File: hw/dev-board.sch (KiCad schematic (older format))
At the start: 66 parts

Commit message: Removed opamp and tied 3.3v LDO switch to sense pin on DC connector.
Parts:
- removed R? (x2): 10K, symbol R
- removed U?: LM358, symbol LM358
- removed X?: RESONATOR, symbol RESONATOR
- added R?: 10K, symbol R
- added X1: CRYSTAL, Spenduino_CustomFootprints:SMD_Crystal_ABM8G, symbol CRYSTAL
- C1, C2, C3, C4, C5, C6, C7, C8, C9: renamed from C?; footprint (none) -> Capacitors_SMD:C_0603
- C10: renamed from 100n; value C -> 100n; footprint (none) -> Capacitors_SMD:C_0603
- D2, D3, D4: renamed from D?; footprint (none) -> LEDs:LED_0603
- F1: renamed from F?; footprint (none) -> Resistors_SMD:R_1812
- IC2, IC6: renamed from IC?; footprint SO8-200 -> (none)
- IC4, IC7: renamed from IC?; footprint WQFN20 -> (none)
- IC5: renamed from IC?; footprint MLF/QFN32 -> (none)
- L1: renamed from L?; footprint (none) -> Resistors_SMD:R_0805
- P1: renamed from P?; footprint (none) -> Spenduino_CustomFootprints:USB_Micro-B_10118194
- P10: renamed from P?; footprint (none) -> Pin_Headers:Pin_Header_Straight_1x06
- P11, P5: renamed from P?; footprint (none) -> Pin_Headers:Pin_Header_Straight_1x08
- P2, P4, P7, P8: renamed from P?; footprint (none) -> pcbfp_lib:Pin_Header_Straight_2x03_ICSP
- P3, P6: renamed from P?; footprint (none) -> pcbfp_lib:Pin_Header_Straight_2x03_ATTINY
- P9: renamed from P?; footprint (none) -> Pin_Headers:Pin_Header_Straight_1x10
- R10, R11, R12, R13, R14, R15, R16, R17, R18, R19, R3, R4, R5, R6, R7, R8, R9: renamed from R?; footprint (none) -> Resistors_SMD:R_0603
- U4: renamed from U?; footprint TQFP-32 -> (none)
- VR1: renamed from VR?; footprint (none) -> Resistors_SMD:R_0603
- VR2: renamed from CG0603MLC-05E; footprint (none) -> Resistors_SMD:R_0603; Part Number (none) -> CG0603MLC-05E1
- X2: renamed from X?; footprint (none) -> Spenduino_CustomFootprints:AWSCR-CV_Resonator
- gave numbers to parts that had none: 10
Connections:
- wire segments 110 -> 107
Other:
- moved on the sheet: C1, C3, C6, C7, C8, D1, P8, Q1, R19, SW1, U2, U3

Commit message: Completed Footprint assignment.
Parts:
- added C11: 47uF, Capacitors_SMD:c_elec_5x5.3, symbol CP
- added C12: 10uF, Capacitors_SMD:c_elec_5x5.3, symbol CP
- C3: value 100n -> .1uF
- C6: value 47u -> 47uF; footprint Capacitors_SMD:C_0603 -> Capacitors_SMD:c_elec_5x5.3
- CON1: footprint (none) -> Connect:BARREL_JACK
- D1: footprint (none) -> GenericTransistorsFoots:SMD_Diode-1206
- IC2, IC6: footprint (none) -> Housings_SOIC:SOIJ-8_5.3x5.3mm_Pitch1.27mm
- IC4, IC7: footprint (none) -> Housings_DFN_QFN:QFN-16-1EP_3x3mm_Pitch0.5mm
- IC5, U4: footprint (none) -> Housings_DFN_QFN:QFN-32-1EP_5x5mm_Pitch0.5mm
- R1: renamed from R?; footprint (none) -> Resistors_SMD:R_0603
- SW1: footprint (none) -> GenericTransistorsFoots:PTS645_Button_SMT
- U3: footprint (none) -> TO_SOT_Packages_SMD:SOT-23-5
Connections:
- wire segments 107 -> 111
- no-connect marks 0 -> 16
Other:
- moved on the sheet: C1, C10, C2, C3, C4, C5, C6, C7, C8, C9, D1, D2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

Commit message: Resolved ERC issues. There are three that remain. They are caused by KiCAD not counting passive pins that conect to a power output.
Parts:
- removed CON1: BARREL_JACK, Connect:BARREL_JACK, symbol BARREL_JACK
- added CON1: BARREL_JACK, Connect:BARREL_JACK, symbol BARREL_JACK_FIXED_PWR
- renumbered U2 to U1, IC7 to U10, U3 to U2, U4 to U3, IC1 to U4, IC2 to U5, IC4 to U6, IC5 to U7, IC3 to U8, IC6 to U9
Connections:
- no-connect marks 16 -> 18
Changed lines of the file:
@@
 $EndDescr
 $Comp
-L ATMEGA16U2 U4
+L ATMEGA16U2 U3
 U 1 1 5756D3EB
 P 4000 2900
-F 0 "U4" H 3150 4250 50  0000 C CNN
+F 0 "U3" H 3150 4250 50  0000 C CNN
 F 1 "ATMEGA16U2" H 4750 1550 50  0000 C CNN
 F 2 "Housings_DFN_QFN:QFN-32-1EP_5x5mm_Pitch0.5mm" H 3850 2950 50  0001 C CNN
@@
 $EndComp
 $Comp
-L MIC5205 U3
+L MIC5205 U2
 U 1 1 575B5F35
 P 3950 8650
-F 0 "U3" H 4150 8300 50  0000 C CNN
+F 0 "U2" H 4150 8300 50  0000 C CNN
 F 1 "MIC5205" H 3950 9100 50  0000 C CNN
 F 2 "TO_SOT_Packages_SMD:SOT-23-5" H 3950 8650 50  0001 C CNN
@@
 $EndComp
 $Comp
-L LM2940LD-5.0 U2
+L LM2940LD-5.0 U1
 U 1 1 57594C2C
 P 3400 7300
-F 0 "U2" H 3175 7575 50  0000 C CNN
+F 0 "U1" H 3600 7100 50  0000 C CNN
 F 1 "LM2940LD-5.0" H 3400 7500 50  0000 C CNN
 F 2 "pcbfp_lib:SOT-223" H 3400 7110 34  0001 C CIN
@@
 $EndComp
 $Comp
-L ATMEGA328PB-MU IC5
+L ATMEGA328PB-MU U7
 U 1 1 575A6773
 P 12150 3450
-F 0 "IC5" H 11400 4700 50  0000 L BNN
+F 0 "U7" H 11400 4700 50  0000 L BNN
 F 1 "ATMEGA328PB-MU" H 12550 2050 50  0000 L BNN
 F 2 "Housings_DFN_QFN:QFN-32-1EP_5x5mm_Pitch0.5mm" H 12800 4700 50  0001 C CIN
@@
 $EndComp
 $Comp
-L ATTINY85-SUR IC2
+L ATTINY85-SUR U5
 U 1 1 575B894B
 P 8600 8950
-F 0 "IC2" H 7450 9350 50  0000 C CNN
+F 0 "U5" H 7450 9350 50  0000 C CNN
 F 1 "ATTINY85-SUR" H 9600 8550 50  0000 C CNN
 F 2 "Housings_SOIC:SOIJ-8_5.3x5.3mm_Pitch1.27mm" H 9550 8950 50  0001 C CIN
@@
 $EndComp
 $Comp
-L 23K256 IC1
+L 23K256 U4
 U 1 1 575B9E25
 P 7900 6250
-F 0 "IC1" H 7350 6550 50  0000 C CNN
+F 0 "U4" H 7350 6550 50  0000 C CNN
 F 1 "23K256" H 8250 5950 50  0000 C CNN
 F 2 "SMD_Packages:SOIC-8-N" H 8100 6550 50  0001 C CIN
@@
 $EndComp
 $Comp
-L TS3A44159 IC4
+L TS3A44159 U6
 U 1 1 575DC855
 P 9750 7650
-F 0 "IC4" H 9400 8300 50  0000 C CNN
+F 0 "U6" H 9400 8300 50  0000 C CNN
 F 1 "TS3A44159" H 9950 7000 50  0000 C CNN
 F 2 "Housings_DFN_QFN:QFN-16-1EP_3x3mm_Pitch0.5mm" H 9775 7650 50  0001 C CIN
@@
 $EndComp
 $Comp
-L ATTINY85-SUR IC6
+L ATTINY85-SUR U9
 U 1 1 575F1949
 P 13250 8950
-F 0 "IC6" H 12100 9350 50  0000 C CNN
+F 0 "U9" H 12100 9350 50  0000 C CNN
 F 1 "ATTINY85-SUR" H 14250 8550 50  0000 C CNN
 F 2 "Housings_SOIC:SOIJ-8_5.3x5.3mm_Pitch1.27mm" H 14200 8950 50  0001 C CIN
@@
 SELECT_T2
 $Comp
-L TS3A44159 IC7
+L TS3A44159 U10
 U 1 1 575F1971
 P 14400 7650
-F 0 "IC7" H 14050 8300 50  0000 C CNN
+F 0 "U10" H 14050 8300 50  0000 C CNN
 F 1 "TS3A44159" H 14600 7000 50  0000 C CNN
 F 2 "Housings_DFN_QFN:QFN-16-1EP_3x3mm_Pitch0.5mm" H 14425 7650 50  0001 C CIN
@@
 IO3_T2
 $Comp
-L BARREL_JACK CON1
-U 1 1 576009D6
-P 2100 7400
-F 0 "CON1" H 2100 7650 50  0000 C CNN
-F 1 "BARREL_JACK" H 2100 7200 50  0000 C CNN
-F 2 "Connect:BARREL_JACK" H 2100 7400 50  0001 C CNN
-F 3 "" H 2100 7400 50  0000 C CNN
-	1    2100 7400
-	1    0    0    -1
-$EndComp
-$Comp
 L D D1
 U 1 1 57600B55
@@
 MOSI1_328
 $Comp
-L 74LVCH1T45 IC3
+L 74LVCH1T45 U8
 U 1 1 5763D0D6
 P 13100 6200
-F 0 "IC3" H 12850 6450 50  0000 C CNN
+F 0 "U8" H 12850 6450 50  0000 C CNN
 F 1 "74LVCH1T45" H 13250 5950 50  0000 C CNN
 F 2 "TO_SOT_Packages_SMD:SOT-886" H 13100 5850 50  0001 C CIN
@@
 L PWR_FLAG #FLG061
 U 1 1 5769BDAE
-P 2450 10100
-F 0 "#FLG061" H 2450 10195 50  0001 C CNN
-F 1 "PWR_FLAG" H 2450 10280 50  0000 C CNN
-F 2 "" H 2450 10100 50  0000 C CNN
-F 3 "" H 2450 10100 50  0000 C CNN
-	1    2450 10100
-	1    0    0    -1
-$EndComp
-$Comp
-L PWR_FLAG #FLG062
-U 1 1 5769BE83
-P 2800 10050
-F 0 "#FLG062" H 2800 10145 50  0001 C CNN
-F 1 "PWR_FLAG" H 2800 10230 50  0000 C CNN
-F 2 "" H 2800 10050 50  0000 C CNN
-F 3 "" H 2800 10050 50  0000 C CNN
-	1    2800 10050
-	-1   0    0    1
-$EndComp
-$Comp
-L PWR_FLAG #FLG063
-U 1 1 5769BF51
-P 2100 10050
-F 0 "#FLG063" H 2100 10145 50  0001 C CNN
-F 1 "PWR_FLAG" H 2100 10230 50  0000 C CNN
-F 2 "" H 2100 10050 50  0000 C CNN
-F 3 "" H 2100 10050 50  0000 C CNN
-	1    2100 10050
-	-1   0    0    1
-$EndComp
-$Comp
-L GND #PWR064
+P 2250 10000
+F 0 "#FLG061" H 2250 10095 50  0001 C CNN
+F 1 "PWR_FLAG" H 2250 10180 50  0000 C CNN
+F 2 "" H 2250 10000 50  0000 C CNN
+F 3 "" H 2250 10000 50  0000 C CNN
+	1    2250 10000
+	1    0    0    -1
+$EndComp
+$Comp
+L GND #PWR062
 U 1 1 5769C1E8
-P 2450 10100
-F 0 "#PWR064" H 2450 9850 50  0001 C CNN
-F 1 "GND" H 2450 9950 50  0000 C CNN
-F 2 "" H 2450 10100 50  0000 C CNN
-F 3 "" H 2450 10100 50  0000 C CNN
-	1    2450 10100
-	1    0    0    -1
-$EndComp
-$Comp
-L +5V #PWR065
-U 1 1 5769C2BF
-P 2100 10050
-F 0 "#PWR065" H 2100 9900 50  0001 C CNN
-F 1 "+5V" H 2100 10190 50  0000 C CNN
-F 2 "" H 2100 10050 50  0000 C CNN
-F 3 "" H 2100 10050 50  0000 C CNN
-	1    2100 10050
-	1    0    0    -1
-$EndComp
-$Comp
-L +3.3V #PWR066
-U 1 1 5769C396
-P 2800 10050
-F 0 "#PWR066" H 2800 9900 50  0001 C CNN
-F 1 "+3.3V" H 2800 10190 50  0000 C CNN
-F 2 "" H 2800 10050 50  0000 C CNN
-F 3 "" H 2800 10050 50  0000 C CNN
-	1    2800 10050
+P 2250 10000
+F 0 "#PWR062" H 2250 9750 50  0001 C CNN
+F 1 "GND" H 2250 9850 50  0000 C CNN
+F 2 "" H 2250 10000 50  0000 C CNN
+F 3 "" H 2250 10000 50  0000 C CNN
+	1    2250 10000
 	1    0    0    -1
 $EndComp
@@
 	4950 8850 4950 8750
 Wire Notes Line
-	1800 9750 3100 9750
+	2650 9650 2650 10250
 Wire Notes Line
-	3100 9750 3100 10350
-Wire Notes Line
-	3100 10350 1800 10350
-Wire Notes Line
-	1800 10350 1800 9750
+	1900 10250 1900 9650
 Wire Notes Line
 	5400 9500 1600 9500
@@
 NoConn ~ 5100 4000
 $Comp
-L GND #PWR?
+L GND #PWR063
 U 1 1 576B8246
 P 10050 2250
-F 0 "#PWR?" H 10050 2000 50  0001 C CNN
+F 0 "#PWR063" H 10050 2000 50  0001 C CNN
 F 1 "GND" H 10050 2100 50  0000 C CNN
 F 2 "" H 10050 2250 50  0000 C CNN
@@
 NoConn ~ 11250 3300
 NoConn ~ 11250 3400
+NoConn ~ 8550 6250
+NoConn ~ 2000 3200
+$Comp
+L BARREL_JACK_FIXED_PWR CON1
+U 1 1 576BF116
+P 2100 7400
+F 0 "CON1" H 2100 7650 50  0000 C CNN
+F 1 "BARREL_JACK" H 2100 7200 50  0000 C CNN
+F 2 "Connect:BARREL_JACK" H 2100 7400 50  0001 C CNN
+F 3 "" H 2100 7400 50  0000 C CNN
+	1    2100 7400
+	1    0    0    -1
+$EndComp
+Wire Notes Line
+	1900 9650 2650 9650
+Wire Notes Line
+	2650 10250 1900 10250
 $EndSCHEMATC

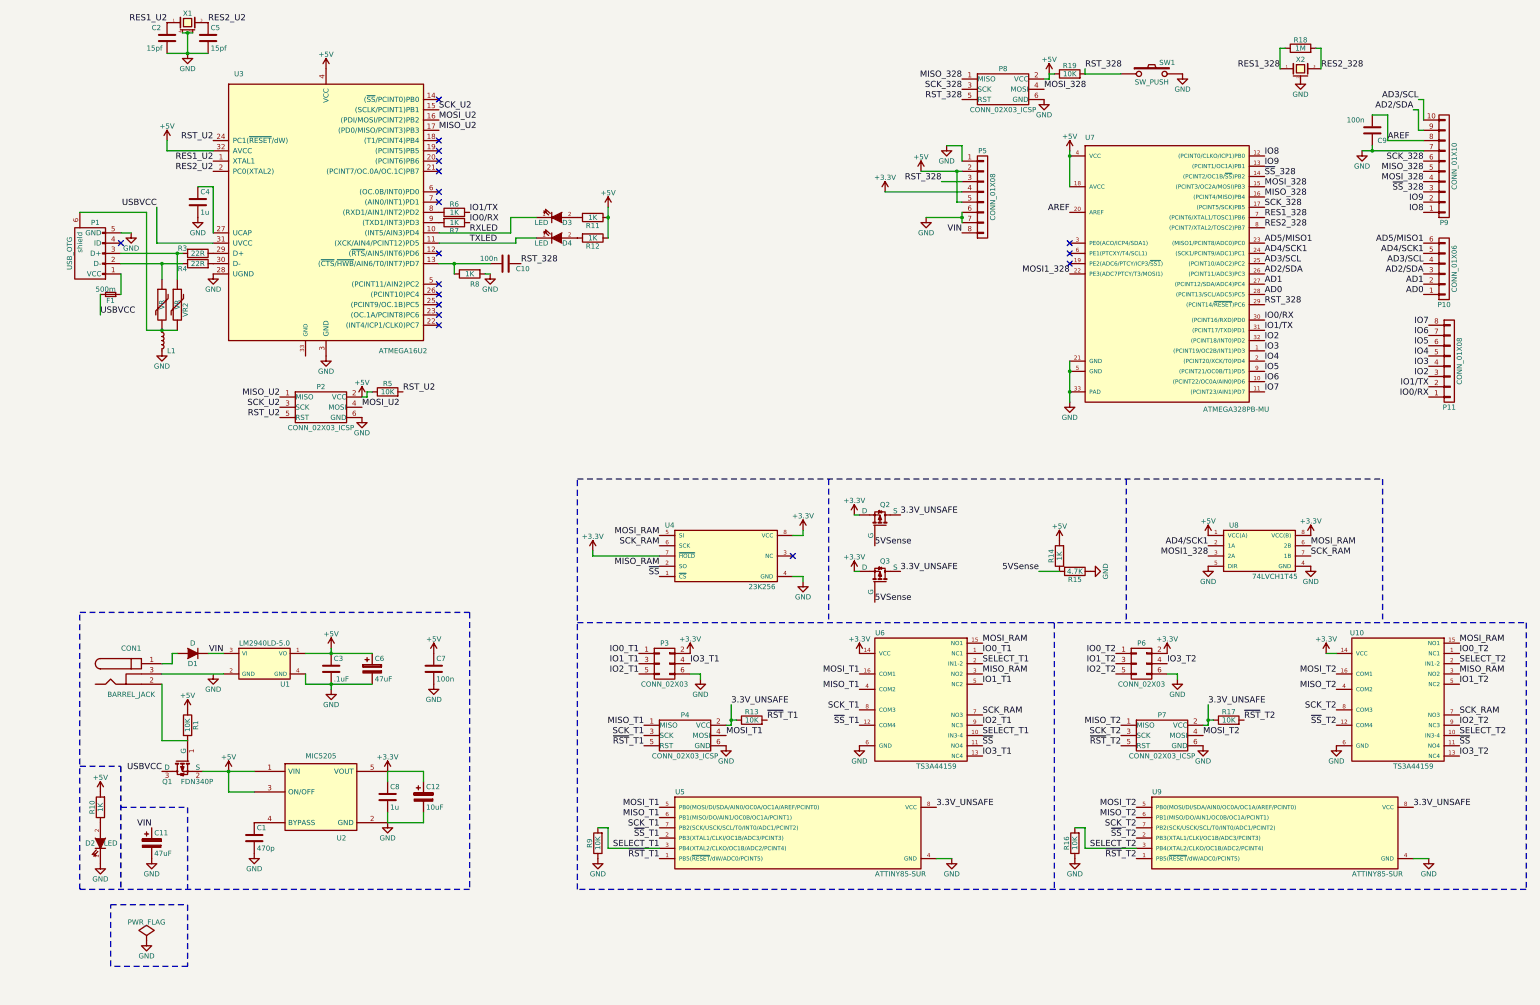
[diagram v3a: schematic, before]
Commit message: Add load switch schematic diagram and fix some wiring.
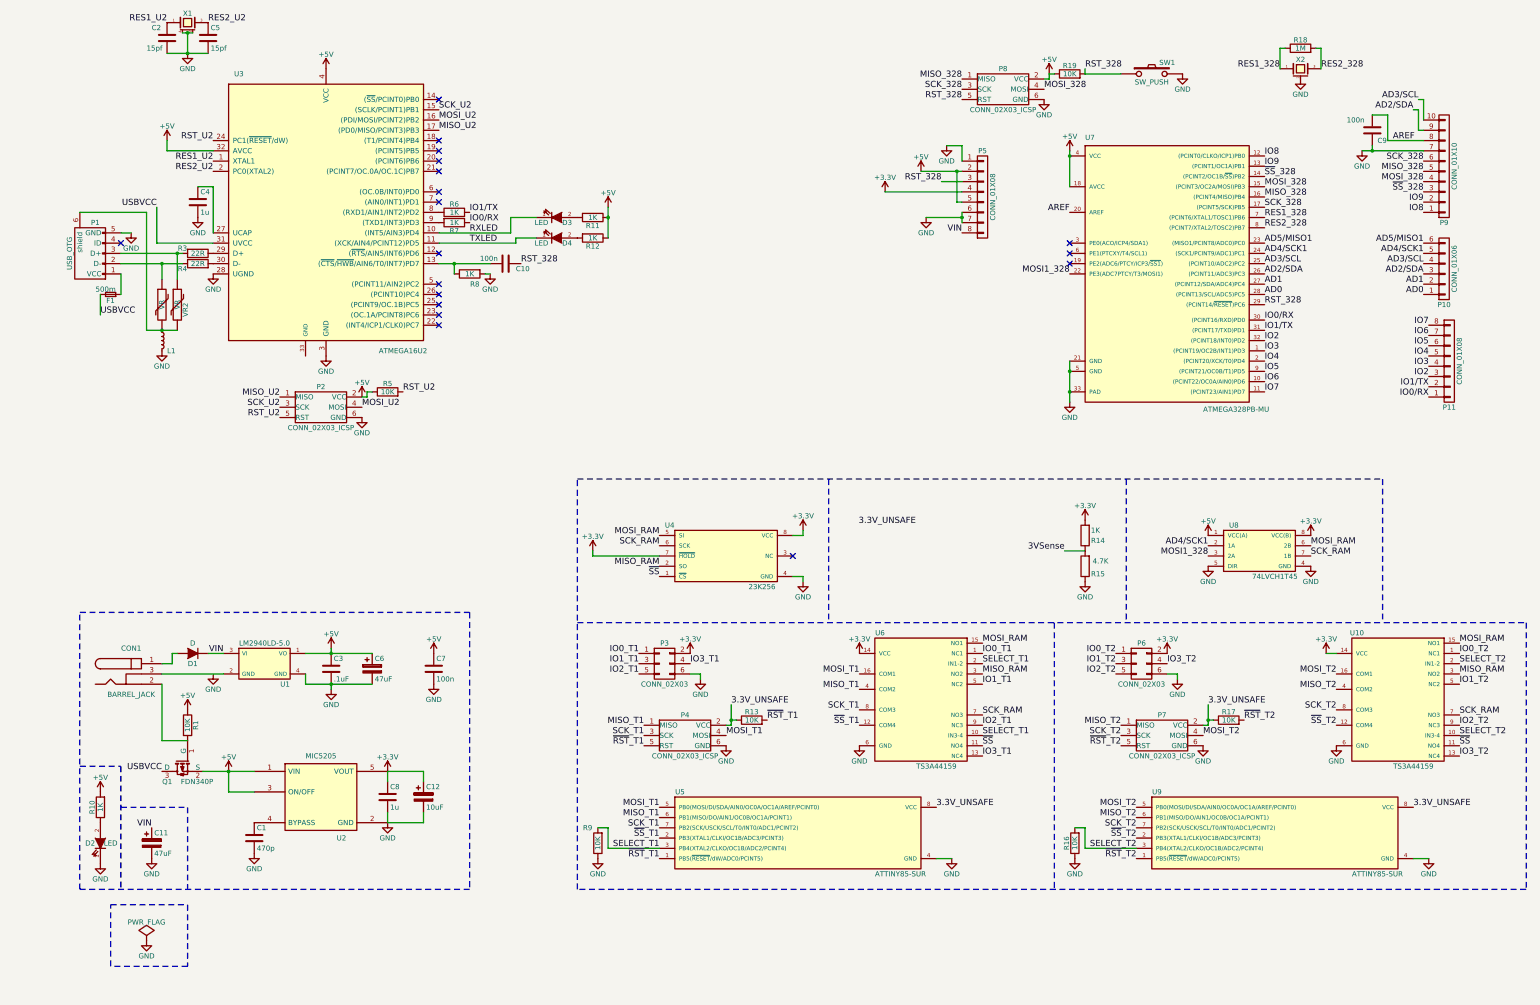
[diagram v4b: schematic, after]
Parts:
- removed Q2, Q3: 2N7002PW, TO_SOT_Packages_SMD:SOT-23, symbol 2N7002PW
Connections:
- net +3V3: now also R14.2
- net +5V: no longer R14.2
- net 5VSense renamed 3VSense
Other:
- moved on the sheet: R14, R15
